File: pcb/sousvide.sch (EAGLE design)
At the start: 10 parts

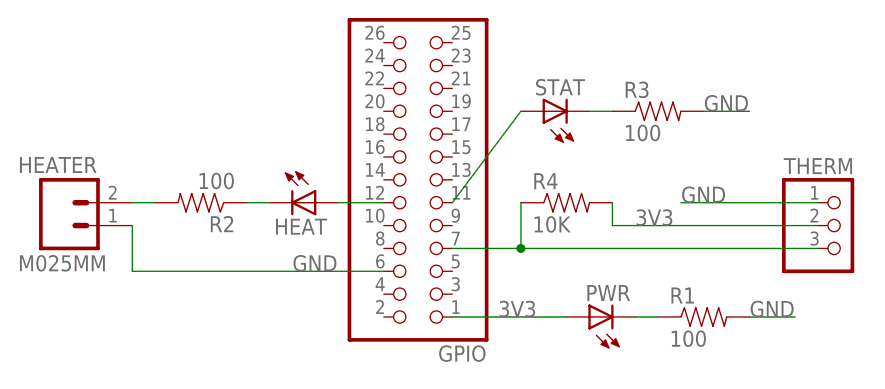
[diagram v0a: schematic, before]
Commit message: Fix bug in PCB.
The first one dropped too much over the LED in line with the heater relay, so
the heater relay never flipped. This removes the LED in line with the heater and
replaces it with an LED on a separate pin.

Important lesson learned: always breadboard your designs before you fab them.
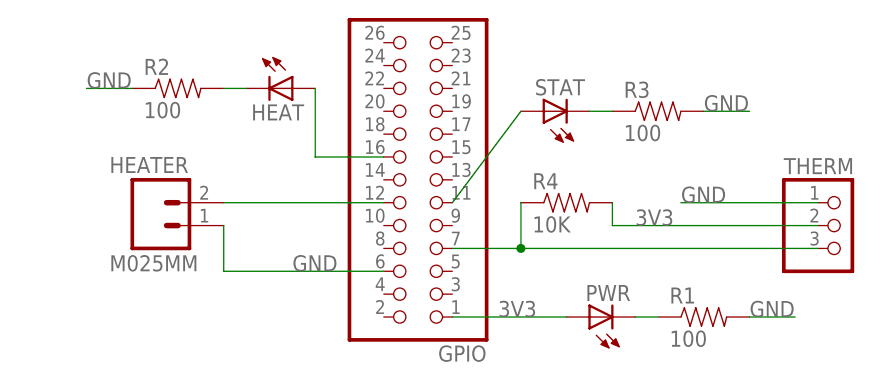
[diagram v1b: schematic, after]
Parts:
- R2: device SparkFun-Passives:RESISTOR1206 -> SparkFun-Resistors:RESISTOR1206
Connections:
- net GND: now also R2.1
- net N$2: now also GPIO.12, HEATER.2; no longer HEAT.C, R2.1
- net N$4: now also GPIO.16, HEAT.A; no longer HEATER.2, R2.2
- net N$5: now also HEAT.C, R2.2; no longer GPIO.12, HEAT.A
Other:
- moved on the sheet: HEAT, HEATER, R2
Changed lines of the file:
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@@
 <part name="HEATER" library="SparkFun-Connectors" deviceset="M02" device="5MM"/>
 <part name="STAT" library="SparkFun-LED" deviceset="LED" device="1206"/>
-<part name="HEAT" library="SparkFun-LED" deviceset="LED" device="1206"/>
 <part name="PWR" library="SparkFun-LED" deviceset="LED" device="1206"/>
 <part name="R1" library="SparkFun-Passives" deviceset="RESISTOR" device="1206" value="100"/>
-<part name="R2" library="SparkFun-Passives" deviceset="RESISTOR" device="1206" value="100"/>
 <part name="R3" library="SparkFun-Passives" deviceset="RESISTOR" device="1206" value="100"/>
 <part name="R4" library="SparkFun-Passives" deviceset="RESISTOR" device="1206" value="10K"/>
+<part name="HEAT" library="SparkFun-LED" deviceset="LED" device="1206"/>
+<part name="R2" library="SparkFun-Resistors" deviceset="RESISTOR" device="1206" value="100"/>
 </parts>
 <sheets>
@@
 <instance part="GPIO" gate="A" x="7.62" y="22.86" rot="R180"/>
 <instance part="THERM" gate="A" x="53.34" y="17.78"/>
-<instance part="HEATER" gate="G$1" x="-33.02" y="17.78" smashed="yes">
-<attribute name="VALUE" x="-38.1" y="12.7" size="1.778" layer="96"/>
-<attribute name="NAME" x="-38.1" y="23.622" size="1.778" layer="95"/>
+<instance part="HEATER" gate="G$1" x="-22.86" y="17.78" smashed="yes">
+<attribute name="VALUE" x="-27.94" y="12.7" size="1.778" layer="96"/>
+<attribute name="NAME" x="-27.94" y="23.622" size="1.778" layer="95"/>
 </instance>
 <instance part="STAT" gate="G$1" x="20.32" y="30.48" rot="R90"/>
-<instance part="HEAT" gate="G$1" x="-5.08" y="20.32" rot="R270"/>
 <instance part="PWR" gate="G$1" x="25.4" y="7.62" rot="R90"/>
 <instance part="R1" gate="G$1" x="38.1" y="7.62"/>
-<instance part="R2" gate="G$1" x="-17.78" y="20.32" rot="R180"/>
 <instance part="R3" gate="G$1" x="33.02" y="30.48"/>
 <instance part="R4" gate="G$1" x="22.86" y="20.32"/>
+<instance part="HEAT" gate="G$1" x="-7.62" y="33.02" rot="R270"/>
+<instance part="R2" gate="G$1" x="-20.32" y="33.02"/>
 </instances>
 <busses>
@@
 <pinref part="R1" gate="G$1" pin="1"/>
 <wire x1="30.48" y1="7.62" x2="33.02" y2="7.62" width="0.1524" layer="91"/>
-</segment>
-</net>
-<net name="N$2" class="0">
-<segment>
-<pinref part="HEAT" gate="G$1" pin="C"/>
-<pinref part="R2" gate="G$1" pin="1"/>
-<wire x1="-10.16" y1="20.32" x2="-12.7" y2="20.32" width="0.1524" layer="91"/>
 </segment>
 </net>
@@
 <segment>
 <pinref part="GPIO" gate="A" pin="6"/>
-<wire x1="2.54" y1="12.7" x2="-25.4" y2="12.7" width="0.1524" layer="91"/>
+<wire x1="2.54" y1="12.7" x2="-15.24" y2="12.7" width="0.1524" layer="91"/>
 <label x="-7.62" y="12.7" size="1.778" layer="95"/>
 <pinref part="HEATER" gate="G$1" pin="1"/>
-<wire x1="-25.4" y1="17.78" x2="-25.4" y2="12.7" width="0.1524" layer="91"/>
+<wire x1="-15.24" y1="17.78" x2="-15.24" y2="12.7" width="0.1524" layer="91"/>
 </segment>
 <segment>
@@
 <label x="35.56" y="20.32" size="1.778" layer="95"/>
 </segment>
-</net>
-<net name="N$4" class="0">
 <segment>
-<pinref part="HEATER" gate="G$1" pin="2"/>
-<pinref part="R2" gate="G$1" pin="2"/>
-<wire x1="-25.4" y1="20.32" x2="-22.86" y2="20.32" width="0.1524" layer="91"/>
-</segment>
-</net>
-<net name="N$5" class="0">
-<segment>
-<pinref part="HEAT" gate="G$1" pin="A"/>
-<pinref part="GPIO" gate="A" pin="12"/>
-<wire x1="-2.54" y1="20.32" x2="2.54" y2="20.32" width="0.1524" layer="91"/>
+<pinref part="R2" gate="G$1" pin="1"/>
+<wire x1="-25.4" y1="33.02" x2="-30.48" y2="33.02" width="0.1524" layer="91"/>
+<label x="-30.48" y="33.02" size="1.778" layer="95"/>
 </segment>
 </net>
@@
 </segment>
 </net>
+<net name="N$2" class="0">
+<segment>
+<pinref part="HEATER" gate="G$1" pin="2"/>
+<pinref part="GPIO" gate="A" pin="12"/>
+<wire x1="-15.24" y1="20.32" x2="2.54" y2="20.32" width="0.1524" layer="91"/>
+</segment>
+</net>
+<net name="N$4" class="0">
+<segment>
+<pinref part="GPIO" gate="A" pin="16"/>
+<wire x1="2.54" y1="25.4" x2="-5.08" y2="25.4" width="0.1524" layer="91"/>
+<pinref part="HEAT" gate="G$1" pin="A"/>
+<wire x1="-5.08" y1="25.4" x2="-5.08" y2="33.02" width="0.1524" layer="91"/>
+</segment>
+</net>
+<net name="N$5" class="0">
+<segment>
+<pinref part="HEAT" gate="G$1" pin="C"/>
+<wire x1="-12.7" y1="33.02" x2="-15.24" y2="33.02" width="0.1524" layer="91"/>
+<pinref part="R2" gate="G$1" pin="2"/>
+</segment>
+</net>
